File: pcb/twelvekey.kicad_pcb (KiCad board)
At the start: 2 copper layers, 75.2 x 62.6 mm, 39 parts, among them J1 Conn_01x06, U1 ATmega328P-AU, U2 SRV05-4, X1 Crystal_GND24_Small

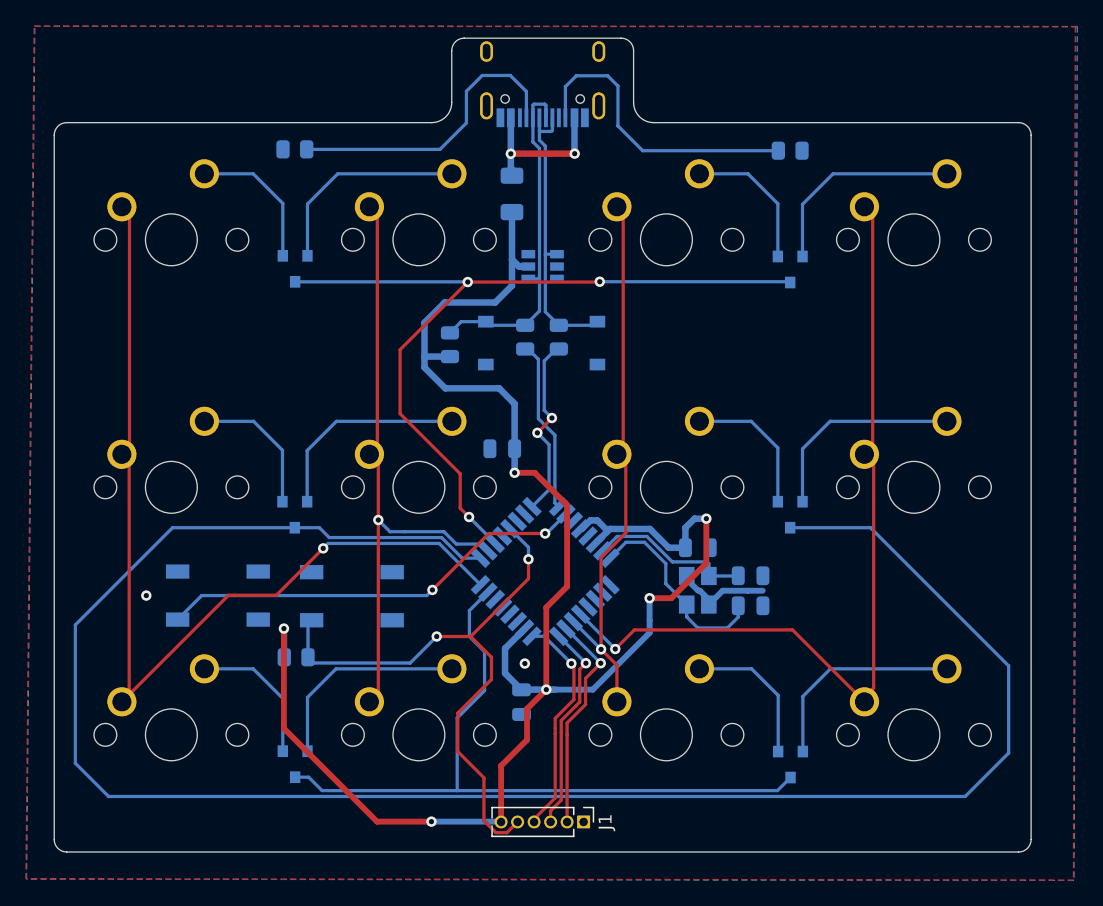
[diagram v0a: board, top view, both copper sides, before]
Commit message: updated PCB to support per-key LEDs
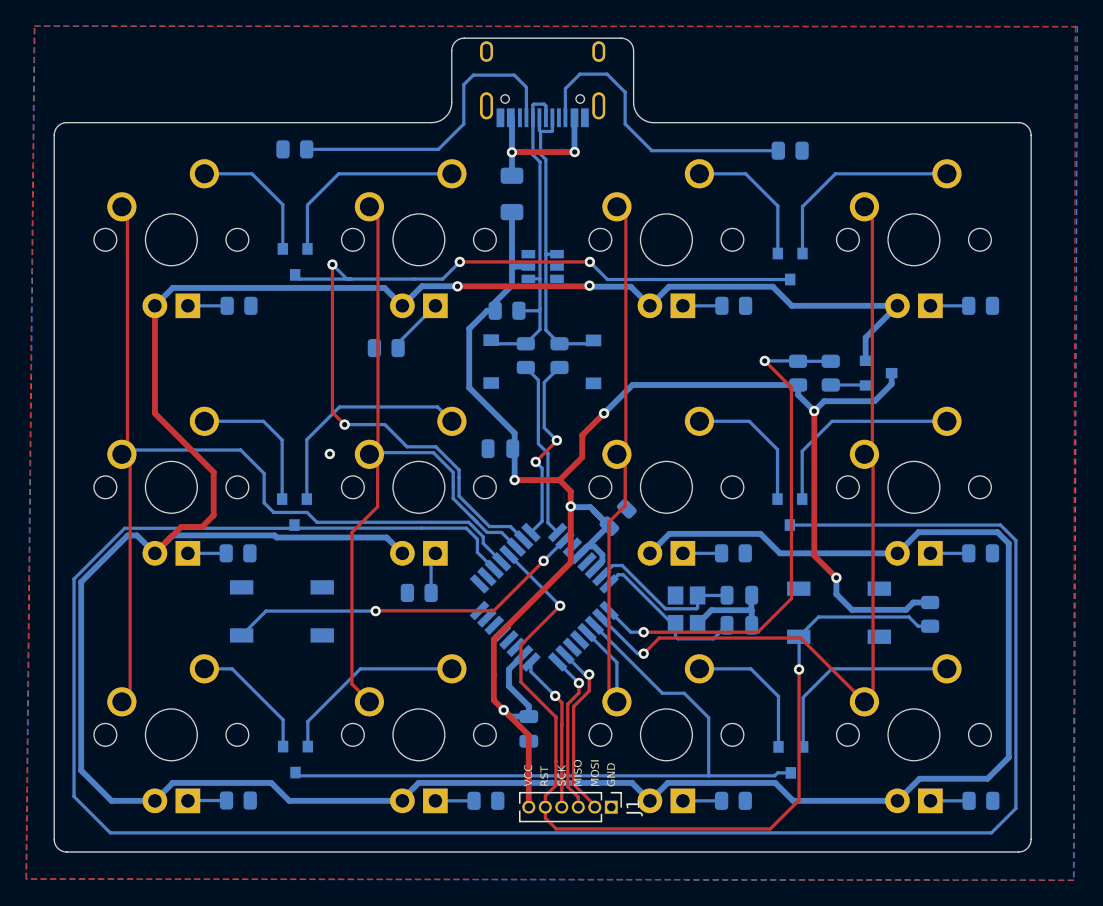
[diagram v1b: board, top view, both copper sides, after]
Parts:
- added Q1: AO3401A, Package_TO_SOT_SMD:SOT-23, B.Cu at (151.2, 64.8)
- added R1: 1k, Resistor_SMD:R_0805_2012Metric, B.Cu at (102.0, 59.6)
- added R10: 1k, Resistor_SMD:R_0805_2012Metric, B.Cu at (159.1, 59.6)
- added R11: 1k, Resistor_SMD:R_0805_2012Metric, B.Cu at (101.9, 78.7)
- added R12: 1k, Resistor_SMD:R_0805_2012Metric, B.Cu at (115.9, 81.7)
- added R13: 1k, Resistor_SMD:R_0805_2012Metric, B.Cu at (140.1, 78.7)
- added R14: 1k, Resistor_SMD:R_0805_2012Metric, B.Cu at (159.1, 78.7)
- added R15: 1k, Resistor_SMD:R_0805_2012Metric, B.Cu at (102.0, 97.7)
- added R16: 1k, Resistor_SMD:R_0805_2012Metric, B.Cu at (121.0, 97.7)
- added R17: 1k, Resistor_SMD:R_0805_2012Metric, B.Cu at (140.1, 97.7)
- added R18: 1k, Resistor_SMD:R_0805_2012Metric, B.Cu at (159.1, 97.7)
- added R19: 100r, Resistor_SMD:R_0805_2012Metric, B.Cu at (147.5, 64.8)
- added R20: 10k, Resistor_SMD:R_0805_2012Metric, B.Cu at (145.0, 64.8)
- added R3: 1k, Resistor_SMD:R_0805_2012Metric, B.Cu at (113.3, 62.9)
- added R4: 1k, Resistor_SMD:R_0805_2012Metric, B.Cu at (140.1, 59.6)
- MX1, MX10, MX11, MX12, MX2, MX3, MX4, MX5, MX6, MX7, MX8, MX9: value MX-NoLED -> MX-LED; footprint MX_Only:MXOnly-1U-NoLED -> MX_Only:MXOnly-1U
- moved R2 48.9 mm to (155.2, 83.4), turned to 90 degrees
- moved RESET 37.5 mm to (148.2, 83.3)
- moved C2 6.56 mm to (131.2, 75.9), turned to 45 degrees
- moved R9 5.12 mm to (122.6, 60.0), turned to 180 degrees
- moved BOOT 5.08 mm to (105.3, 83.2)
- moved J1 2.42 mm to (130.7, 98.2)
- moved C3 2.13 mm to (124.3, 92.2)
- moved U1 1.98 mm to (125.5, 82.1)
- moved C8 1.73 mm to (140.5, 81.9)
- moved C7 1.73 mm to (140.5, 84.2)
- moved X1 1.73 mm to (136.4, 83.0)
- moved D8 1.48 mm to (129.3, 64.0)
- moved D7 1.48 mm to (121.4, 63.9)
- moved R7 1.42 mm to (124.1, 63.5)
- moved R8 1.42 mm to (126.7, 63.5)
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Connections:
- U1 pad 10: Net-(U1-Pad10) -> col3
- U1 pad 11: Net-(U1-Pad11) -> row2
- U1 pad 12: Net-(U1-Pad12) -> col2
- U1 pad 13: col3 -> Net-(U1-Pad13)
- U1 pad 14: col2 -> Net-(U1-Pad14)
- U1 pad 23: row2 -> Net-(U1-Pad23)
- U1 pad 24: col0 -> Net-(U1-Pad24)
- U1 pad 25: row1 -> Net-(U1-Pad25)
- U1 pad 26: col1 -> Net-(U1-Pad26)
- U1 pad 27: row0 -> row1
- U1 pad 28: Net-(U1-Pad28) -> col0
- U1 pad 30: Net-(U1-Pad30) -> col1
- U1 pad 31: Net-(U1-Pad31) -> row0
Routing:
- net LED+: track 0.00 -> 255.8 mm, vias 0 -> 2
- net Net-(R19-Pad2): track 0.00 -> 40.0 mm, vias 0 -> 2
- net RESET: track 47.3 -> 69.0 mm
- net row1: track 148.1 -> 165.7 mm
- net row0: track 63.5 -> 72.6 mm, vias 3 -> 4
- net col1: track 49.6 -> 56.5 mm, vias 1 -> 0
- net +5V: track 139.1 -> 133.2 mm
- net BOOT: track 33.3 -> 27.9 mm
- net SCK: track 17.6 -> 12.3 mm
- net Net-(MX2-Pad4): track 0.00 -> 4.44 mm
- net MISO: track 16.4 -> 12.6 mm
- net Net-(C7-Pad1): track 15.8 -> 12.4 mm
- net MOSI: track 17.1 -> 13.9 mm
- net Net-(MX6-Pad4): track 0.00 -> 3.19 mm
- net Net-(MX1-Pad4): track 0.00 -> 3.02 mm
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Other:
- board text added: "GND"
- board text added: "MISO"
- board text added: "MOSI"
- board text added: "RST"
- board text added: "SCK"
- board text added: "VCC"

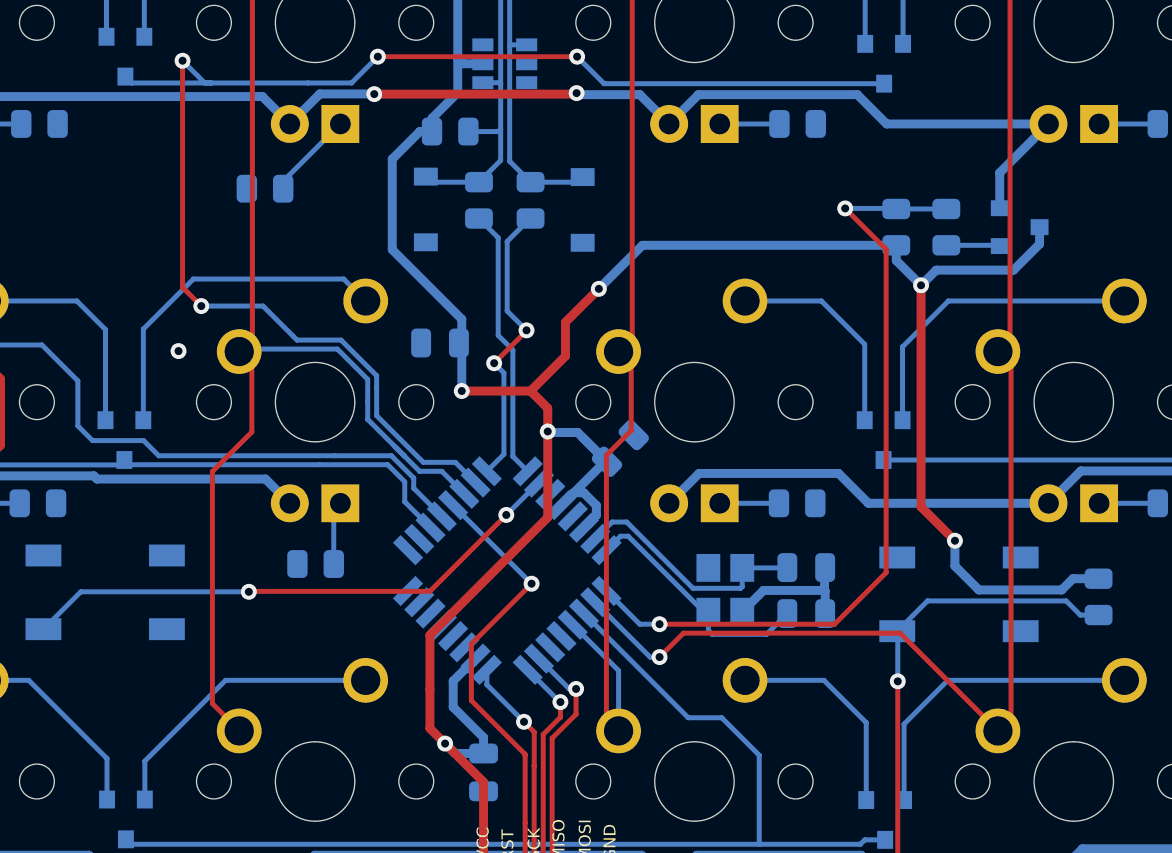
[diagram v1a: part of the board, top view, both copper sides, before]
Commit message: fix backlight
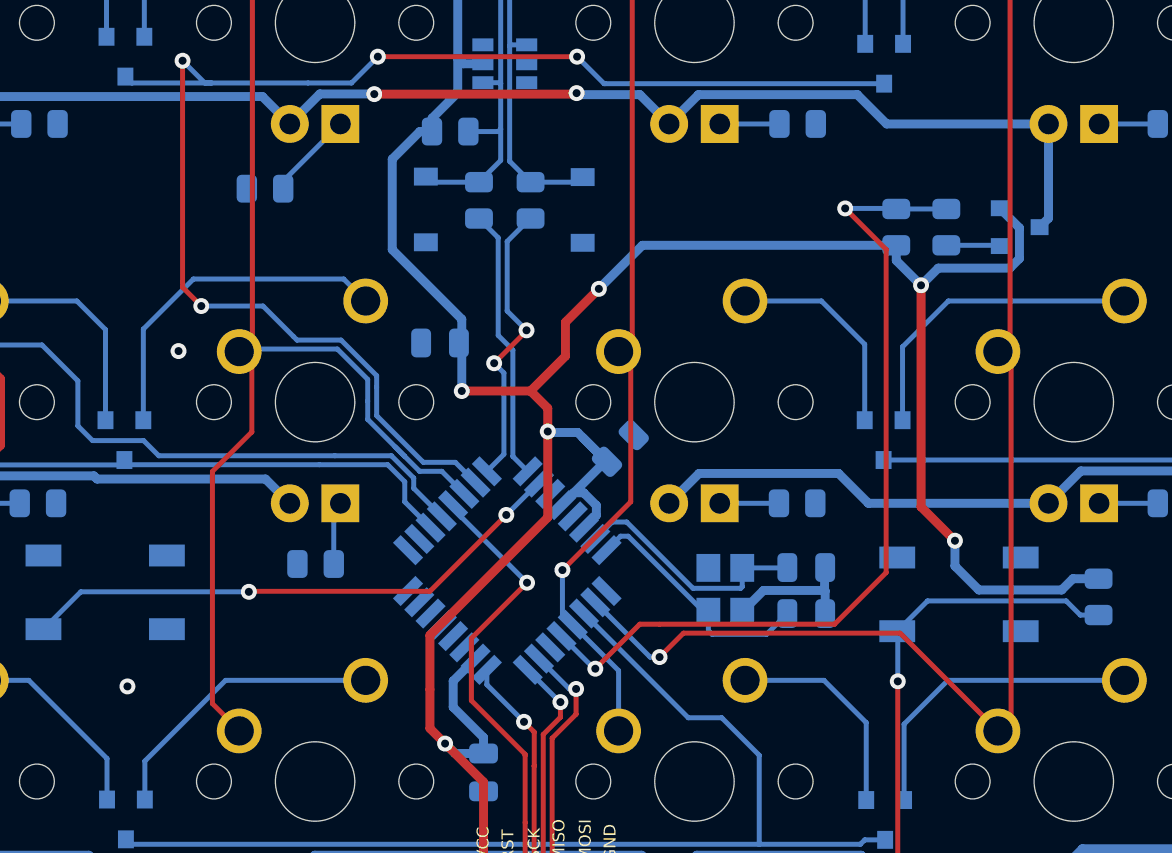
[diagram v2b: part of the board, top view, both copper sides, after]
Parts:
- renumbered BOOT to BOOT1, RESET to RESET1
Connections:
- Q1 pad 2: LED+ -> +5V
- Q1 pad 3: +5V -> LED+
- U1 pad 13: Net-(U1-Pad13) -> Net-(R19-Pad2)
- U1 pad 9: Net-(R19-Pad2) -> Net-(U1-Pad9)
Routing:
- net col2: track 46.0 -> 41.5 mm, vias 0 -> 1
- net Net-(R19-Pad2): track 40.0 -> 43.2 mm
- net +5V: track 133.2 -> 134.0 mm
- net GND: vias 1 -> 2

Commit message: update images
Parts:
- renumbered BOOT1 to BOOT, RESET1 to RESET
